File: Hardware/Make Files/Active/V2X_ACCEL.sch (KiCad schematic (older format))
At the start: 6 parts, among them Q1 BSS84, U1 ADXL345

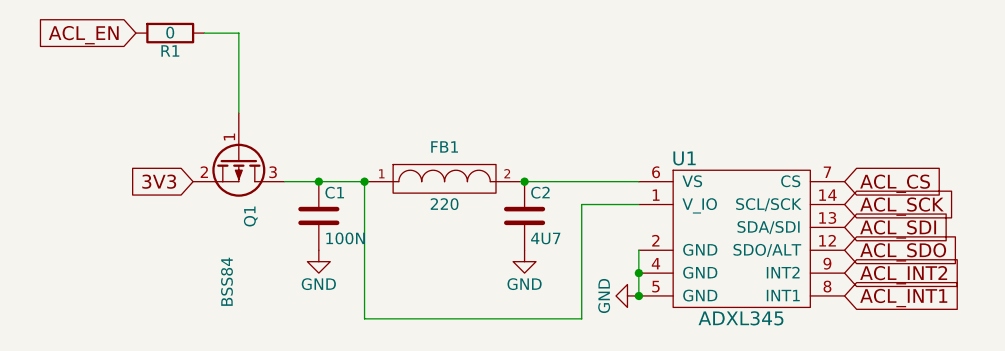
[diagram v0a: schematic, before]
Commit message: Saving V1.1 as archive.
We are trying a new architecture where the FTDI can be removed. making a
backup spot
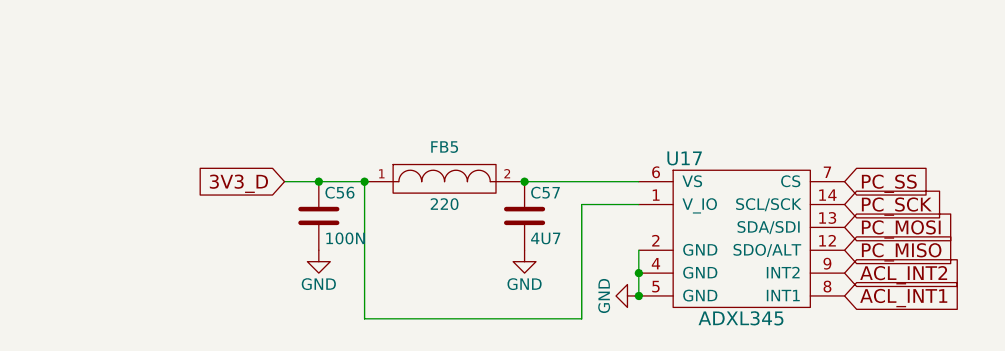
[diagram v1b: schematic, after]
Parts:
- removed Q1: BSS84, Housings_SOT-23_SOT-143_TSOT-6:SOT-23, symbol Q_PMOS_GSD
- removed R1: 0, Resistors_SMD:R_0603, symbol R
- C56: renamed from C1; Mouse PN (none) -> http://www.mouser.com/ds/2/400/mlcc_commercial_general_en-2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
- C57: renamed from C2; Mouse PN (none) -> 963-LMK212B7475KG-T
- FB5: renamed from FB1; Mouse PN (none) -> 810-MPZ1608S221ATA00
- U17: renamed from U1; Mouse PN (none) -> 584-ADXL345BCCZ-R7
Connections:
- net 3V3_D: now reaches C56.1, FB5.1, U17.1 (V_IO)
- net ACL_CS renamed PC_SS
- net ACL_SCK renamed PC_SCK
- net ACL_SDI renamed PC_MOSI
- net ACL_SDO renamed PC_MISO
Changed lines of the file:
@@
 $EndDescr
 $Comp
-L ADXL345 U1
+L ADXL345 U17
 U 1 1 55B56FB6
 P 6400 3550
-F 0 "U1" H 6150 4050 60  0000 C CNN
+F 0 "U17" H 6150 4050 60  0000 C CNN
 F 1 "ADXL345" H 6400 3350 60  0000 C CNN
 F 2 "Custom Parts:LGA-14_5x3mm" H 6400 3550 60  0001 C CNN
-F 3 "" H 6400 3550 60  0000 C CNN
+F 3 "http://www.mouser.com/ds/2/609/ADXL345-246395.pdf" H 6400 3550 60  0001 C CNN
+F 4 "584-ADXL345BCCZ-R7" H 6400 3550 60  0001 C CNN "Mouse PN"
 	1    6400 3550
 	1    0    0    -1
 $EndComp
 $Comp
-L GND #PWR0119
+L GND #PWR117
 U 1 1 55B570DE
 P 5950 3650
-F 0 "#PWR0119" H 5950 3400 50  0001 C CNN
+F 0 "#PWR117" H 5950 3400 50  0001 C CNN
 F 1 "GND" H 5950 3500 50  0000 C CNN
 F 2 "" H 5950 3650 60  0000 C CNN
@@
 Connection ~ 5950 3650
 $Comp
-L GND #PWR0120
+L GND #PWR115
 U 1 1 55B57118
 P 4550 3450
-F 0 "#PWR0120" H 4550 3200 50  0001 C CNN
+F 0 "#PWR115" H 4550 3200 50  0001 C CNN
 F 1 "GND" H 4550 3300 50  0000 C CNN
 F 2 "" H 4550 3450 60  0000 C CNN
@@
 $EndComp
 $Comp
-L C C1
+L C C56
 U 1 1 55B57121
 P 4550 3300
-F 0 "C1" H 4575 3400 50  0000 L CNN
+F 0 "C56" H 4575 3400 50  0000 L CNN
 F 1 "100N" H 4575 3200 50  0000 L CNN
 F 2 "Capacitors_SMD:C_0603" H 4588 3150 30  0001 C CNN
-F 3 "" H 4550 3300 60  0000 C CNN
+F 3 "http://www.mouser.com/ds/2/400/mlcc_commercial_general_en-266370.pdf" H 4550 3300 60  0001 C CNN
+F 4 "http://www.mouser.com/ds/2/400/mlcc_commercial_general_en-266370.pdf" H 4550 3300 60  0001 C CNN "Mouse PN"
 	1    4550 3300
 	1    0    0    -1
 $EndComp
 $Comp
-L C C2
+L C C57
 U 1 1 55B571B1
 P 5450 3300
-F 0 "C2" H 5475 3400 50  0000 L CNN
+F 0 "C57" H 5475 3400 50  0000 L CNN
 F 1 "4U7" H 5475 3200 50  0000 L CNN
 F 2 "Capacitors_SMD:C_0603" H 5488 3150 30  0001 C CNN
-F 3 "" H 5450 3300 60  0000 C CNN
+F 3 "http://www.yuden.co.jp/productdata/catalog/en/mlcc_all_e.pdf" H 5450 3300 60  0001 C CNN
+F 4 "963-LMK212B7475KG-T" H 5450 3300 60  0001 C CNN "Mouse PN"
 	1    5450 3300
 	1    0    0    -1
 $EndComp
 $Comp
-L FILTER FB1
+L FILTER FB5
 U 1 1 55B571EB
 P 5100 3150
-F 0 "FB1" H 5100 3300 50  0000 C CNN
+F 0 "FB5" H 5100 3300 50  0000 C CNN
 F 1 "220" H 5100 3050 50  0000 C CNN
 F 2 "Capacitors_SMD:C_0805" H 5100 3150 60  0001 C CNN
-F 3 "" H 5100 3150 60  0000 C CNN
+F 3 "http://product.tdk.com/emc/beads/detailed_information.php?lang=en&ref=jp&part_no=MPZ1608S221ATA00" H 5100 3150 60  0001 C CNN
+F 4 "810-MPZ1608S221ATA00" H 5100 3150 60  0001 C CNN "Mouse PN"
 	1    5100 3150
 	1    0    0    -1
@@
 	5450 3150 5950 3150
 $Comp
-L GND #PWR0121
+L GND #PWR116
 U 1 1 55B57242
 P 5450 3450
-F 0 "#PWR0121" H 5450 3200 50  0001 C CNN
+F 0 "#PWR116" H 5450 3200 50  0001 C CNN
 F 1 "GND" H 5450 3300 50  0000 C CNN
 F 2 "" H 5450 3450 60  0000 C CNN
@@
 	1    0    0    -1
 $EndComp
-Wire Wire Line
-	4400 3150 4750 3150
 Connection ~ 4750 3150
-$Comp
-L Q_PMOS_GSD Q1
-U 1 1 55C4A050
-P 4200 3050
-F 0 "Q1" H 4500 3100 50  0000 R CNN
-F 1 "BSS84" H 4850 3000 50  0000 R CNN
-F 2 "Housings_SOT-23_SOT-143_TSOT-6:SOT-23" H 4400 3150 29  0001 C CNN
-F 3 "" H 4200 3050 60  0000 C CNN
-	1    4200 3050
-	0    1    1    0
-$EndComp
 Wire Wire Line
 	4750 3150 4750 3750
@@
 Connection ~ 5450 3150
 Connection ~ 4550 3150
-Text GLabel 4000 3150 0    60   Input ~ 0
-3V3
-Text GLabel 6850 3150 2    60   Input ~ 0
-ACL_CS
-Text GLabel 6850 3250 2    60   Input ~ 0
-ACL_SCK
-Text GLabel 6850 3350 2    60   Input ~ 0
-ACL_SDI
-Text GLabel 6850 3450 2    60   Input ~ 0
-ACL_SDO
 Text GLabel 6850 3550 2    60   Input ~ 0
 ACL_INT2
 Text GLabel 6850 3650 2    60   Input ~ 0
 ACL_INT1
-$Comp
-L R R1
-U 1 1 55C4213E
-P 3900 2500
-F 0 "R1" V 3980 2500 50  0000 C CNN
-F 1 "0" V 3900 2500 50  0000 C CNN
-F 2 "Resistors_SMD:R_0603" V 3830 2500 30  0001 C CNN
-F 3 "" H 3900 2500 30  0000 C CNN
-	1    3900 2500
-	0    1    1    0
-$EndComp
-Text GLabel 3750 2500 0    60   Input ~ 0
-ACL_EN
+Text GLabel 4400 3150 0    60   Input ~ 0
+3V3_D
 Wire Wire Line
-	4200 2500 4200 2850
-Wire Wire Line
-	4050 2500 4200 2500
+	4400 3150 4750 3150
+Text GLabel 6850 3250 2    60   Input ~ 0
+PC_SCK
+Text GLabel 6850 3450 2    60   Input ~ 0
+PC_MISO
+Text GLabel 6850 3350 2    60   Input ~ 0
+PC_MOSI
+Text GLabel 6850 3150 2    60   Input ~ 0
+PC_SS
 $EndSCHEMATC

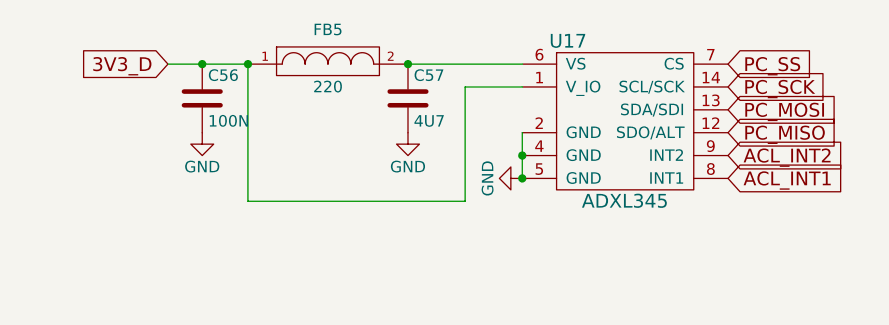
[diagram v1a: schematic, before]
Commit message: V1.2 mostly done
BOM is integrated and creates mouser orders
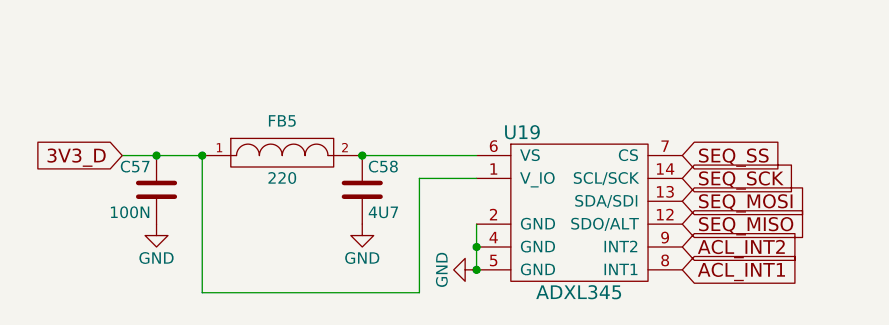
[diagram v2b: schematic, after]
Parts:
- removed C56: 100N, Capacitors_SMD:C_0603, symbol C
- added C57: 100N, Capacitors_SMD:C_0603, symbol C
- renumbered C57 to C58, U17 to U19
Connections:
- net 3V3_D: now also C57.1
- net GND: now also C57.2
- net PC_MISO renamed SEQ_MISO
- net PC_MOSI renamed SEQ_MOSI
- net PC_SCK renamed SEQ_SCK
- net PC_SS renamed SEQ_SS
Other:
- moved on the sheet: C58, FB5, U19
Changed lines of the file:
@@
 encoding utf-8
 Sheet 6 8
-Title "OBD2-SMS - Open source RVI over SMS daughter card"
+Title "V2X - Open source RVI over SMS daughter card"
 Date "2015-07-17"
-Rev "0.01"
-Comp "Jaguar Land Rover"
+Rev "1.2"
+Comp "Jaguar Land Rover OSTC"
 Comment1 "Designer: Jesse Banks"
 Comment2 "Advisor: Rudolf Steif"
@@
 $EndDescr
 $Comp
-L ADXL345 U17
+L ADXL345 U19
 U 1 1 55B56FB6
-P 6400 3550
-F 0 "U17" H 6150 4050 60  0000 C CNN
-F 1 "ADXL345" H 6400 3350 60  0000 C CNN
-F 2 "Custom Parts:LGA-14_5x3mm" H 6400 3550 60  0001 C CNN
-F 3 "http://www.mouser.com/ds/2/609/ADXL345-246395.pdf" H 6400 3550 60  0001 C CNN
-F 4 "584-ADXL345BCCZ-R7" H 6400 3550 60  0001 C CNN "Mouse PN"
-	1    6400 3550
+P 6200 3950
+F 0 "U19" H 5950 4450 60  0000 C CNN
+F 1 "ADXL345" H 6200 3750 60  0000 C CNN
+F 2 "Custom Parts:LGA-14_5x3mm" H 6200 3950 60  0001 C CNN
+F 3 "http://www.mouser.com/ds/2/609/ADXL345-246395.pdf" H 6200 3950 60  0001 C CNN
+F 4 "584-ADXL345BCCZ-R7" H 6200 3950 60  0001 C CNN "Mouse PN"
+	1    6200 3950
 	1    0    0    -1
 $EndComp
 $Comp
-L GND #PWR117
+L GND #PWR0120
 U 1 1 55B570DE
-P 5950 3650
-F 0 "#PWR117" H 5950 3400 50  0001 C CNN
-F 1 "GND" H 5950 3500 50  0000 C CNN
-F 2 "" H 5950 3650 60  0000 C CNN
-F 3 "" H 5950 3650 60  0000 C CNN
-	1    5950 3650
+P 5750 4050
+F 0 "#PWR0120" H 5750 3800 50  0001 C CNN
+F 1 "GND" H 5750 3900 50  0000 C CNN
+F 2 "" H 5750 4050 60  0000 C CNN
+F 3 "" H 5750 4050 60  0000 C CNN
+	1    5750 4050
 	0    1    1    0
 $EndComp
 Wire Wire Line
-	5950 3450 5950 3650
-Connection ~ 5950 3550
-Connection ~ 5950 3650
+	5750 3850 5750 4050
+Connection ~ 5750 3950
+Connection ~ 5750 4050
 $Comp
-L GND #PWR115
+L GND #PWR0121
 U 1 1 55B57118
-P 4550 3450
-F 0 "#PWR115" H 4550 3200 50  0001 C CNN
-F 1 "GND" H 4550 3300 50  0000 C CNN
-F 2 "" H 4550 3450 60  0000 C CNN
-F 3 "" H 4550 3450 60  0000 C CNN
-	1    4550 3450
+P 4350 3850
+F 0 "#PWR0121" H 4350 3600 50  0001 C CNN
+F 1 "GND" H 4350 3700 50  0000 C CNN
+F 2 "" H 4350 3850 60  0000 C CNN
+F 3 "" H 4350 3850 60  0000 C CNN
+	1    4350 3850
 	1    0    0    -1
 $EndComp
 $Comp
-L C C56
-U 1 1 55B57121
-P 4550 3300
-F 0 "C56" H 4575 3400 50  0000 L CNN
-F 1 "100N" H 4575 3200 50  0000 L CNN
-F 2 "Capacitors_SMD:C_0603" H 4588 3150 30  0001 C CNN
-F 3 "http://www.mouser.com/ds/2/400/mlcc_commercial_general_en-266370.pdf" H 4550 3300 60  0001 C CNN
-F 4 "http://www.mouser.com/ds/2/400/mlcc_commercial_general_en-266370.pdf" H 4550 3300 60  0001 C CNN "Mouse PN"
-	1    4550 3300
-	1    0    0    -1
-$EndComp
-$Comp
-L C C57
+L C C58
 U 1 1 55B571B1
-P 5450 3300
-F 0 "C57" H 5475 3400 50  0000 L CNN
-F 1 "4U7" H 5475 3200 50  0000 L CNN
-F 2 "Capacitors_SMD:C_0603" H 5488 3150 30  0001 C CNN
-F 3 "http://www.yuden.co.jp/productdata/catalog/en/mlcc_all_e.pdf" H 5450 3300 60  0001 C CNN
-F 4 "963-LMK212B7475KG-T" H 5450 3300 60  0001 C CNN "Mouse PN"
-	1    5450 3300
+P 5250 3700
+F 0 "C58" H 5275 3800 50  0000 L CNN
+F 1 "4U7" H 5275 3600 50  0000 L CNN
+F 2 "Capacitors_SMD:C_0603" H 5288 3550 30  0001 C CNN
+F 3 "http://www.yuden.co.jp/productdata/catalog/en/mlcc_all_e.pdf" H 5250 3700 60  0001 C CNN
+F 4 "963-LMK212B7475KG-T" H 5250 3700 60  0001 C CNN "Mouse PN"
+	1    5250 3700
 	1    0    0    -1
 $EndComp
@@
 L FILTER FB5
 U 1 1 55B571EB
-P 5100 3150
-F 0 "FB5" H 5100 3300 50  0000 C CNN
-F 1 "220" H 5100 3050 50  0000 C CNN
-F 2 "Capacitors_SMD:C_0805" H 5100 3150 60  0001 C CNN
-F 3 "http://product.tdk.com/emc/beads/detailed_information.php?lang=en&ref=jp&part_no=MPZ1608S221ATA00" H 5100 3150 60  0001 C CNN
-F 4 "810-MPZ1608S221ATA00" H 5100 3150 60  0001 C CNN "Mouse PN"
-	1    5100 3150
+P 4900 3550
+F 0 "FB5" H 4900 3700 50  0000 C CNN
+F 1 "220" H 4900 3450 50  0000 C CNN
+F 2 "Capacitors_SMD:C_0805" H 4900 3550 60  0001 C CNN
+F 3 "http://product.tdk.com/emc/beads/detailed_information.php?lang=en&ref=jp&part_no=MPZ1608S221ATA00" H 4900 3550 60  0001 C CNN
+F 4 "810-MPZ1608S221ATA00" H 4900 3550 60  0001 C CNN "Mouse PN"
+	1    4900 3550
 	1    0    0    -1
 $EndComp
 Wire Wire Line
-	5450 3150 5950 3150
+	5250 3550 5750 3550
 $Comp
-L GND #PWR116
+L GND #PWR0122
 U 1 1 55B57242
-P 5450 3450
-F 0 "#PWR116" H 5450 3200 50  0001 C CNN
-F 1 "GND" H 5450 3300 50  0000 C CNN
-F 2 "" H 5450 3450 60  0000 C CNN
-F 3 "" H 5450 3450 60  0000 C CNN
-	1    5450 3450
+P 5250 3850
+F 0 "#PWR0122" H 5250 3600 50  0001 C CNN
+F 1 "GND" H 5250 3700 50  0000 C CNN
+F 2 "" H 5250 3850 60  0000 C CNN
+F 3 "" H 5250 3850 60  0000 C CNN
+	1    5250 3850
 	1    0    0    -1
 $EndComp
-Connection ~ 4750 3150
+Connection ~ 4550 3550
 Wire Wire Line
-	4750 3150 4750 3750
+	4550 3550 4550 4150
 Wire Wire Line
-	4750 3750 5700 3750
+	4550 4150 5500 4150
 Wire Wire Line
-	5700 3750 5700 3250
+	5500 4150 5500 3650
 Wire Wire Line
-	5700 3250 5950 3250
-Connection ~ 5450 3150
-Connection ~ 4550 3150
-Text GLabel 6850 3550 2    60   Input ~ 0
+	5500 3650 5750 3650
+Connection ~ 5250 3550
+Connection ~ 4350 3550
+Text GLabel 6650 3950 2    60   Input ~ 0
 ACL_INT2
-Text GLabel 6850 3650 2    60   Input ~ 0
+Text GLabel 6650 4050 2    60   Input ~ 0
 ACL_INT1
-Text GLabel 4400 3150 0    60   Input ~ 0
+Text GLabel 4200 3550 0    60   Input ~ 0
 3V3_D
 Wire Wire Line
-	4400 3150 4750 3150
-Text GLabel 6850 3250 2    60   Input ~ 0
-PC_SCK
-Text GLabel 6850 3450 2    60   Input ~ 0
-PC_MISO
-Text GLabel 6850 3350 2    60   Input ~ 0
-PC_MOSI
-Text GLabel 6850 3150 2    60   Input ~ 0
-PC_SS
+	4200 3550 4550 3550
+Text GLabel 6650 3650 2    60   Input ~ 0
+SEQ_SCK
+Text GLabel 6650 3850 2    60   Input ~ 0
+SEQ_MISO
+Text GLabel 6650 3750 2    60   Input ~ 0
+SEQ_MOSI
+Text GLabel 6650 3550 2    60   Input ~ 0
+SEQ_SS
+$Comp
+L C C57
+U 1 1 5605F70E
+P 4350 3700
+F 0 "C57" H 4375 3800 50  0000 L CNN
+F 1 "100N" H 4375 3600 50  0000 L CNN
+F 2 "Capacitors_SMD:C_0603" H 4388 3550 30  0001 C CNN
+F 3 "http://www.mouser.com/ds/2/400/mlcc_commercial_general_en-266370.pdf" H 4350 3700 60  0001 C CNN
+F 4 "810-C1608X7R1E104K" H 4350 3700 60  0001 C CNN "Mouse PN"
+	1    4350 3700
+	-1   0    0    -1
+$EndComp
 $EndSCHEMATC

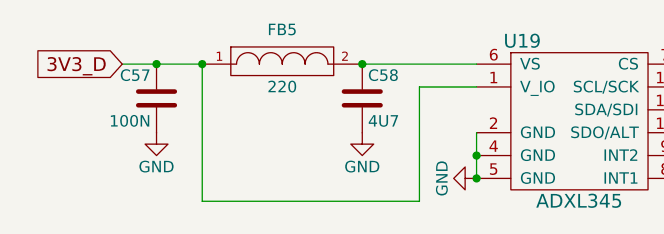
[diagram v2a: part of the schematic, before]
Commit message: V2X v1.2 sch and bom
Made changes to the schematic to V1.2 (remove FTDI possibly) and
integrade the BOM information into the sch
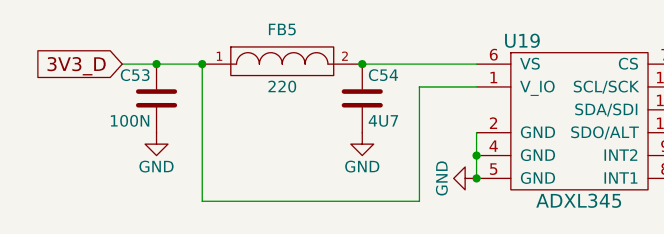
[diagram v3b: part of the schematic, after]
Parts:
- renumbered C57 to C53, C58 to C54
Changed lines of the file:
@@
 $EndComp
 $Comp
-L GND #PWR0120
+L GND #PWR121
 U 1 1 55B570DE
 P 5750 4050
-F 0 "#PWR0120" H 5750 3800 50  0001 C CNN
+F 0 "#PWR121" H 5750 3800 50  0001 C CNN
 F 1 "GND" H 5750 3900 50  0000 C CNN
 F 2 "" H 5750 4050 60  0000 C CNN
@@
 Connection ~ 5750 4050
 $Comp
-L GND #PWR0121
+L GND #PWR119
 U 1 1 55B57118
 P 4350 3850
-F 0 "#PWR0121" H 4350 3600 50  0001 C CNN
+F 0 "#PWR119" H 4350 3600 50  0001 C CNN
 F 1 "GND" H 4350 3700 50  0000 C CNN
 F 2 "" H 4350 3850 60  0000 C CNN
@@
 $EndComp
 $Comp
-L C C58
+L C C54
 U 1 1 55B571B1
 P 5250 3700
-F 0 "C58" H 5275 3800 50  0000 L CNN
+F 0 "C54" H 5275 3800 50  0000 L CNN
 F 1 "4U7" H 5275 3600 50  0000 L CNN
 F 2 "Capacitors_SMD:C_0603" H 5288 3550 30  0001 C CNN
@@
 	5250 3550 5750 3550
 $Comp
-L GND #PWR0122
+L GND #PWR120
 U 1 1 55B57242
 P 5250 3850
-F 0 "#PWR0122" H 5250 3600 50  0001 C CNN
+F 0 "#PWR120" H 5250 3600 50  0001 C CNN
 F 1 "GND" H 5250 3700 50  0000 C CNN
 F 2 "" H 5250 3850 60  0000 C CNN
@@
 SEQ_SS
 $Comp
-L C C57
+L C C53
 U 1 1 5605F70E
 P 4350 3700
-F 0 "C57" H 4375 3800 50  0000 L CNN
+F 0 "C53" H 4375 3800 50  0000 L CNN
 F 1 "100N" H 4375 3600 50  0000 L CNN
 F 2 "Capacitors_SMD:C_0603" H 4388 3550 30  0001 C CNN

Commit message: Split V2X in 2 boards, layout of SIM pcb done
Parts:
- C53: footprint Capacitors_SMD:C_0603 -> Custom Parts:C_0603_SM
- C54: footprint Capacitors_SMD:C_0603 -> Custom Parts:C_0805_SM
- FB5: footprint Capacitors_SMD:C_0805 -> Custom Parts:R_0603_sm
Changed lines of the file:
@@
 EESchema Schematic File Version 2
+LIBS:V2X-rescue
+LIBS:sim5320_KICAD_PART
+LIBS:CUSTOM_KICAD_PART
+LIBS:74xgxx
+LIBS:74xx
+LIBS:ac-dc
+LIBS:actel
+LIBS:adc-dac
+LIBS:Altera
+LIBS:analog_devices
+LIBS:analog_switches
+LIBS:atmel
+LIBS:audio
+LIBS:brooktre
+LIBS:cmos_ieee
+LIBS:cmos4000
+LIBS:conn
+LIBS:contrib
+LIBS:cypress
+LIBS:dc-dc
+LIBS:device
+LIBS:digital-audio
+LIBS:diode
+LIBS:display
+LIBS:dsp
+LIBS:elec-unifil
+LIBS:ESD_Protection
+LIBS:ftdi
+LIBS:gennum
+LIBS:graphic
+LIBS:hc11
+LIBS:intel
+LIBS:interface
+LIBS:ir
+LIBS:Lattice
+LIBS:linear
+LIBS:logo
+LIBS:maxim
+LIBS:memory
+LIBS:microchip
+LIBS:microchip_dspic33dsc
+LIBS:microchip_pic10mcu
+LIBS:microchip_pic12mcu
+LIBS:microchip_pic16mcu
+LIBS:microchip_pic18mcu
+LIBS:microchip_pic32mcu
+LIBS:microcontrollers
+LIBS:motor_drivers
+LIBS:motorola
+LIBS:msp430
+LIBS:nordicsemi
+LIBS:nxp_armmcu
+LIBS:onsemi
+LIBS:opto
+LIBS:Oscillators
+LIBS:philips
 LIBS:power
-LIBS:device
+LIBS:Power_Management
+LIBS:powerint
+LIBS:pspice
+LIBS:references
+LIBS:regul
+LIBS:relays
+LIBS:rfcom
+LIBS:sensors
+LIBS:silabs
+LIBS:siliconi
+LIBS:stm8
+LIBS:stm32
+LIBS:supertex
+LIBS:switches
+LIBS:texas
+LIBS:transf
 LIBS:transistors
-LIBS:conn
-LIBS:linear
-LIBS:regul
-LIBS:74xx
-LIBS:cmos4000
-LIBS:adc-dac
-LIBS:memory
+LIBS:ttl_ieee
+LIBS:valves
+LIBS:video
+LIBS:Xicor
 LIBS:xilinx
-LIBS:microcontrollers
-LIBS:dsp
-LIBS:microchip
-LIBS:analog_switches
-LIBS:motorola
-LIBS:texas
-LIBS:intel
-LIBS:audio
-LIBS:interface
-LIBS:digital-audio
-LIBS:philips
-LIBS:display
-LIBS:cypress
-LIBS:siliconi
-LIBS:opto
-LIBS:atmel
-LIBS:contrib
-LIBS:valves
-LIBS:sim5320_KICAD_PART
-LIBS:dc-dc
-LIBS:CUSTOM_KICAD_PART
+LIBS:Zilog
 LIBS:V2X-cache
 EELAYER 25 0
@@
 $EndComp
 $Comp
-L GND #PWR121
+L GND #PWR0128
 U 1 1 55B570DE
 P 5750 4050
-F 0 "#PWR121" H 5750 3800 50  0001 C CNN
+F 0 "#PWR0128" H 5750 3800 50  0001 C CNN
 F 1 "GND" H 5750 3900 50  0000 C CNN
 F 2 "" H 5750 4050 60  0000 C CNN
@@
 Connection ~ 5750 4050
 $Comp
-L GND #PWR119
+L GND #PWR0129
 U 1 1 55B57118
 P 4350 3850
-F 0 "#PWR119" H 4350 3600 50  0001 C CNN
+F 0 "#PWR0129" H 4350 3600 50  0001 C CNN
 F 1 "GND" H 4350 3700 50  0000 C CNN
 F 2 "" H 4350 3850 60  0000 C CNN
@@
 F 0 "C54" H 5275 3800 50  0000 L CNN
 F 1 "4U7" H 5275 3600 50  0000 L CNN
-F 2 "Capacitors_SMD:C_0603" H 5288 3550 30  0001 C CNN
+F 2 "Custom Parts:C_0805_SM" H 5288 3550 30  0001 C CNN
 F 3 "http://www.yuden.co.jp/productdata/catalog/en/mlcc_all_e.pdf" H 5250 3700 60  0001 C CNN
 F 4 "963-LMK212B7475KG-T" H 5250 3700 60  0001 C CNN "Mouse PN"
@@
 F 0 "FB5" H 4900 3700 50  0000 C CNN
 F 1 "220" H 4900 3450 50  0000 C CNN
-F 2 "Capacitors_SMD:C_0805" H 4900 3550 60  0001 C CNN
+F 2 "Custom Parts:R_0603_sm" H 4900 3550 60  0001 C CNN
 F 3 "http://product.tdk.com/emc/beads/detailed_information.php?lang=en&ref=jp&part_no=MPZ1608S221ATA00" H 4900 3550 60  0001 C CNN
 F 4 "810-MPZ1608S221ATA00" H 4900 3550 60  0001 C CNN "Mouse PN"
@@
 	5250 3550 5750 3550
 $Comp
-L GND #PWR120
+L GND #PWR0130
 U 1 1 55B57242
 P 5250 3850
-F 0 "#PWR120" H 5250 3600 50  0001 C CNN
+F 0 "#PWR0130" H 5250 3600 50  0001 C CNN
 F 1 "GND" H 5250 3700 50  0000 C CNN
 F 2 "" H 5250 3850 60  0000 C CNN
@@
 F 0 "C53" H 4375 3800 50  0000 L CNN
 F 1 "100N" H 4375 3600 50  0000 L CNN
-F 2 "Capacitors_SMD:C_0603" H 4388 3550 30  0001 C CNN
+F 2 "Custom Parts:C_0603_SM" H 4388 3550 30  0001 C CNN
 F 3 "http://www.mouser.com/ds/2/400/mlcc_commercial_general_en-266370.pdf" H 4350 3700 60  0001 C CNN
 F 4 "810-C1608X7R1E104K" H 4350 3700 60  0001 C CNN "Mouse PN"
